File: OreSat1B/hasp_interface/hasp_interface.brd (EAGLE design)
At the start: 83 x 100 mm, 63 parts, among them J1 SAMTEC-MMS-104-02-X-SHJ, J2 ORESAT-DEBUG-CONNECTOR-ALL, J3 MOLEX-43045XXXXVERTICAL, U1 TCAN330, U10 TPS63070, U3 OKI-T/36W-W40, U7 STM32F091C, X1 16MHZ-2.5x2mm

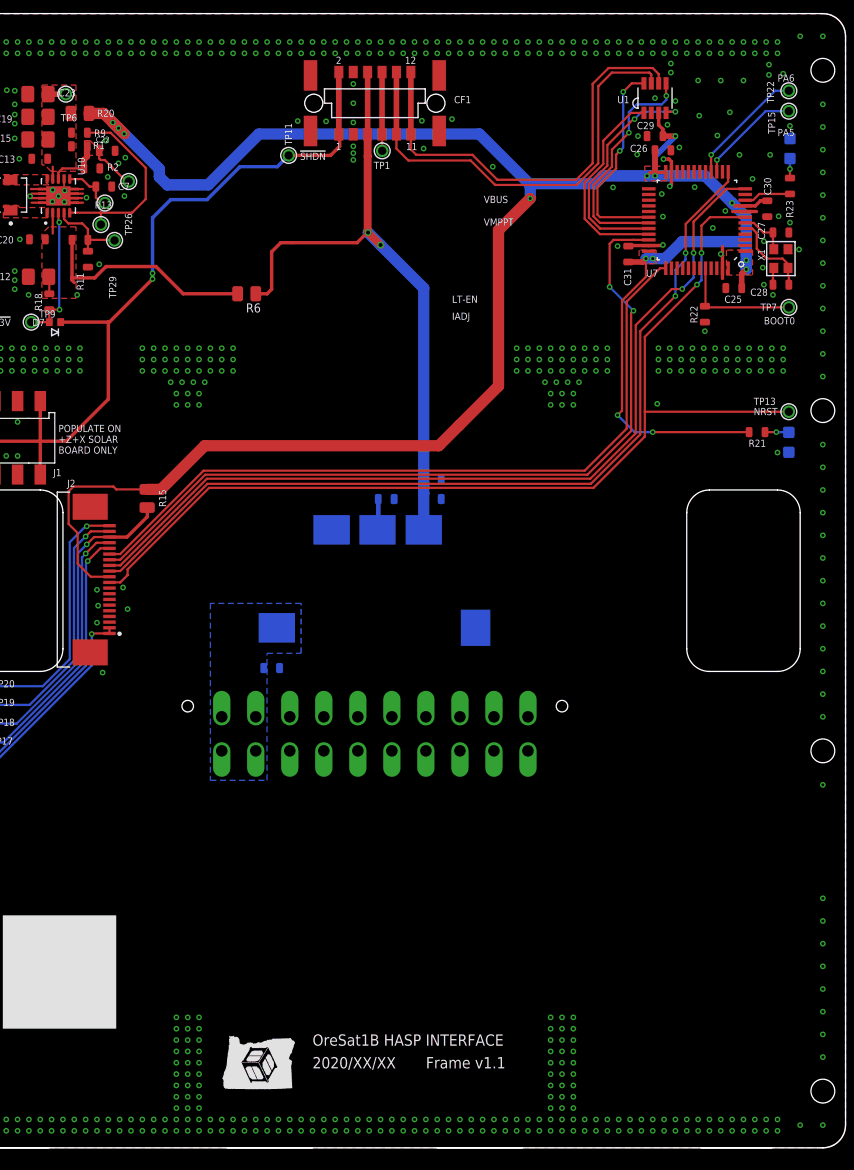
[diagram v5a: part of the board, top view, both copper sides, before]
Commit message: Added RS232 level converter in case we want it. Added DAC outputs to HASP analog inputs in case we want it. Moved main connector out of fastener's way. Cleanup.
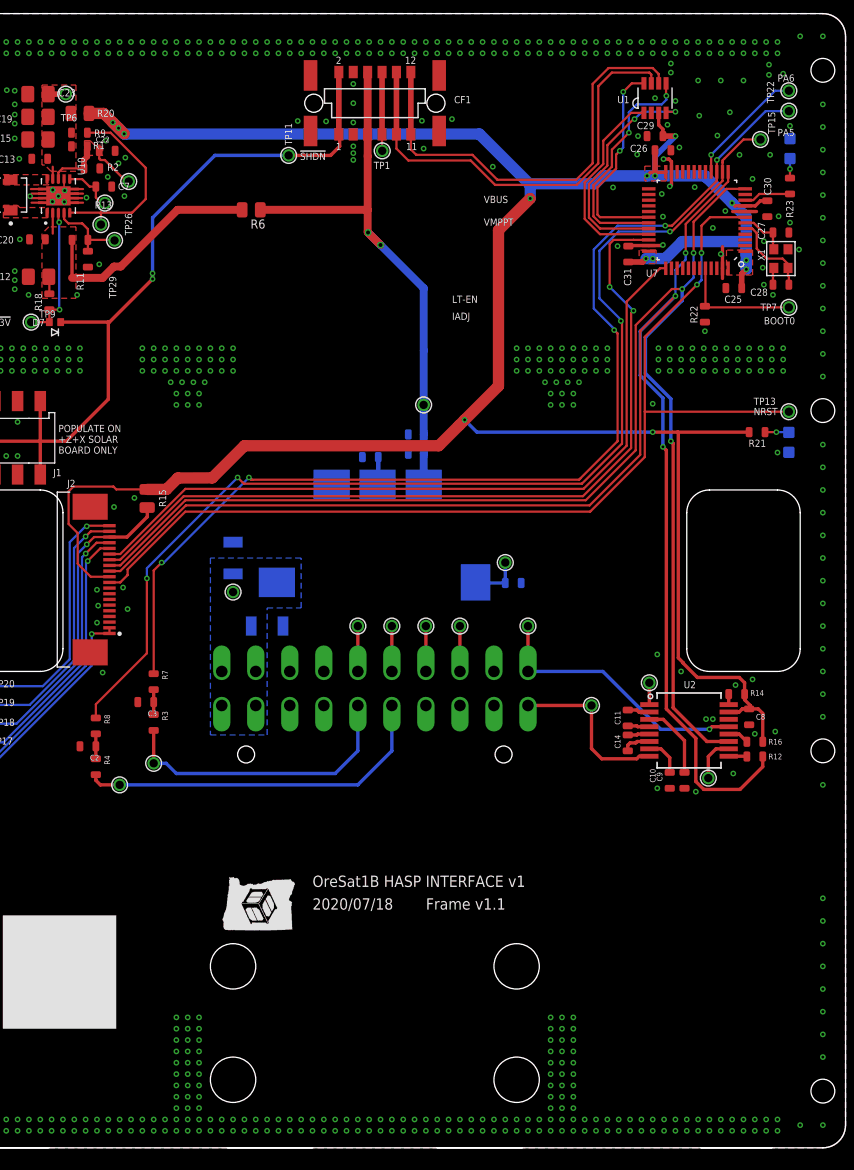
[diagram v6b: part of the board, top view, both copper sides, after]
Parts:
- added C10, C11, C14, C8, C9: 100n, oresat-rcl:.0603-C-NOSILK
- added C2, C3, R3, R4, R7, R8: NP, oresat-rcl:.0603-C-NOSILK
- added C4: 10u 60V, oresat-rcl:1206-C
- added R10: 3.8k, oresat-rcl:.0603-C-NOSILK
- added R12, R14, R16: 10k, oresat-rcl:.0603-C-NOSILK
- added TP10, TP12, TP14, TP16, TP2, TP23, TP24, TP25, TP3, TP30, TP31, TP32, TP4, TP5: TEST-POINT-LARGE-SQUARE, oresat-misc:1X01
- added U2: MAX3227EEAE/V+, U-Maxim-MAX3227-RS232-transceiver-driver:21-0056_A16+2_MXM
- C1: value 10u / 75V -> 10U 60V; device oresat-rcl:.0603-C-NOSILK -> oresat-rcl:1206-C
- J3: value MOLEX-43045XXXXVERTICAL -> MOLEX-43045XXXXRIGHTANGLE; device J-Molex-043045XXXX-Dual-Row-Connector:0430452012 -> J-Molex-043045XXXX-Dual-Row-Connector:0430452000
- U3: value OKI-T/36W-W40 -> OKI-T/36W-W40N
- moved R6 7.41 mm to (30.6, 82.7)
- moved C5 4.27 mm to (45.1, 61.2), turned to 0 degrees
- moved C6 4.27 mm to (45.1, 62.9), turned to 0 degrees
- moved J3 4.00 mm to (41.5, 40.5)
- moved U3 4.00 mm to (41.5, 54.0)
- moved R5 3.96 mm to (41.1, 60.9), turned to 180 degrees
- moved C1 3.72 mm to (32.0, 46.0)
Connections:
- removed net PA5: TP15.1, U7.15
- new net N$10: C14.1, U2.5
- new net N$11: C11.2, U2.4
- new net N$12: C11.1, U2.2
- new net N$13: R12.1, U2.9
- new net N$15: R16.1, U2.12
- new net N$17: TP31.1, U2.10
- new net N$18: TP32.1, U2.1
- new net N$3: C3.1, R3.1, R7.2
- new net N$4: C2.1, R4.1, R8.2
- new net N$5: R10.2, TP30.1, U3.1
- new net N$6: R14.1, U2.16
- new net N$7: C10.1, U2.7
- new net N$8: C9.1, U2.3
- new net N$9: C14.2, U2.6
- new net PA4/DAC0: R8.1, TP25.1, U7.14
- new net PA5/DAC1: R7.1, TP15.1, U7.15
- net +30VDC: now also C4.1, TP2.1
- net 3.3V: now also C8.1, R14.2, R16.2, U2.15
- net GND: now also C10.2, C2.2, C3.2, C4.2, C8.2, C9.2, J3.13, J3.14, J3.19, J3.3, J3.4, R10.1, U2.14; no longer J3.17, J3.18, J3.5, J3.6, U3.1
- net HASP_ANALOG_1: now also J3.6, R4.2, TP5.1; no longer J3.4
- net HASP_ANALOG_2: now also J3.5, R3.2, TP4.1; no longer J3.3
- net HASP_DISCRETE_1: now also J3.18, TP14.1; no longer J3.16
- net HASP_DISCRETE_2: now also J3.17, TP16.1; no longer J3.15
- net HASP_DISCRETE_3: now also J3.16, TP23.1; no longer J3.14
- net HASP_DISCRETE_4: now also J3.15, TP24.1; no longer J3.13
- net HASP_SERIAL_RX: now also TP12.1, U2.13
- net HASP_SERIAL_TX: now also TP10.1, U2.8
- net PA2/USART2_TX: now also U2.11
- net PA3/USART2_RX: now also R12.2
- net VBUS: now also TP3.1
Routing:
- net PA4/DAC0: track 0.00 -> 99.3 mm, vias 0 -> 4
- net PA5/DAC1: track 0.00 -> 96.0 mm, vias 0 -> 5
- net PA3/USART2_RX: track 78.1 -> 133.2 mm, vias 2 -> 3
- net PA2/USART2_TX: track 78.3 -> 124.6 mm, vias 2 -> 3
- net HASP_ANALOG_1: track 0.00 -> 32.0 mm
- net 3.3V: track 200.9 -> 230.2 mm
- net HASP_ANALOG_2: track 0.00 -> 26.1 mm
- net HASP_SERIAL_RX: track 0.00 -> 23.9 mm, vias 0 -> 1
- net HASP_SERIAL_TX: track 0.00 -> 15.0 mm
- net VBUS: track 59.3 -> 49.5 mm
- net PA5: track 9.18 -> 0.00 mm, vias 1 -> 0
- net N$8: track 0.00 -> 6.68 mm
- net N$5: track 0.00 -> 5.04 mm
- net HASP_DISCRETE_4: track 0.00 -> 4.00 mm
- net HASP_DISCRETE_3: track 0.00 -> 4.00 mm
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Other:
- board text added: "2020/07/18"
- board text added: "2021/07/18"
- board text added: "OreSat1B HASP INTERFACE v1"
- board text added: "OreSat1B HASP Interface v1"
- board text removed: "2020/12/15"
- board text removed: "2020/XX/XX"
- board text removed: "OreSat Solar Module v5.1"
- board text removed: "OreSat1B HASP INTERFACE"
